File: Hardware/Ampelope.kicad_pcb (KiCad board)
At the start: 2 copper layers, 18.8 x 110 mm, 35 parts, among them J1 IN_A, J2 IN_B, J3 RM_OUT, J4 Eurorack_10_pin_power, U1 MC1496, U2 TL072

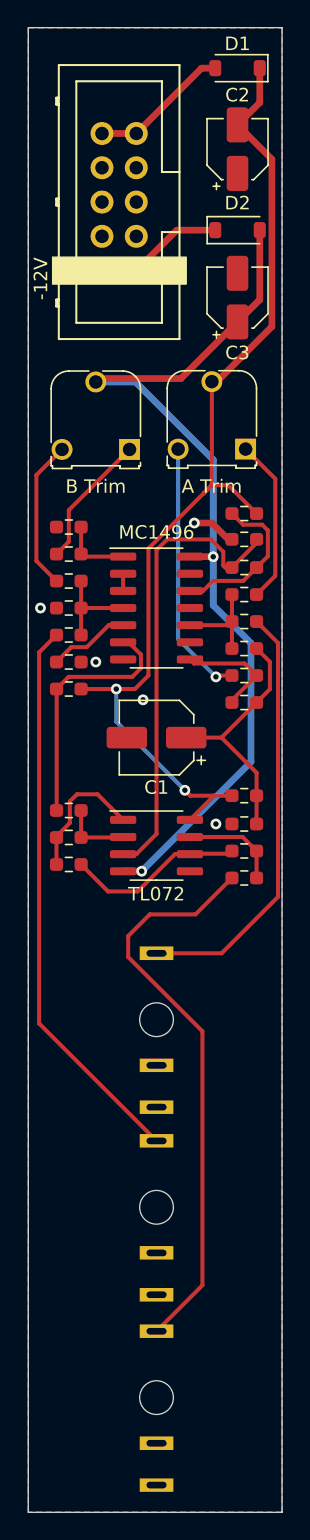
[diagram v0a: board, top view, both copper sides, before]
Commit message: Added STM32G431 project; clock configuration complete
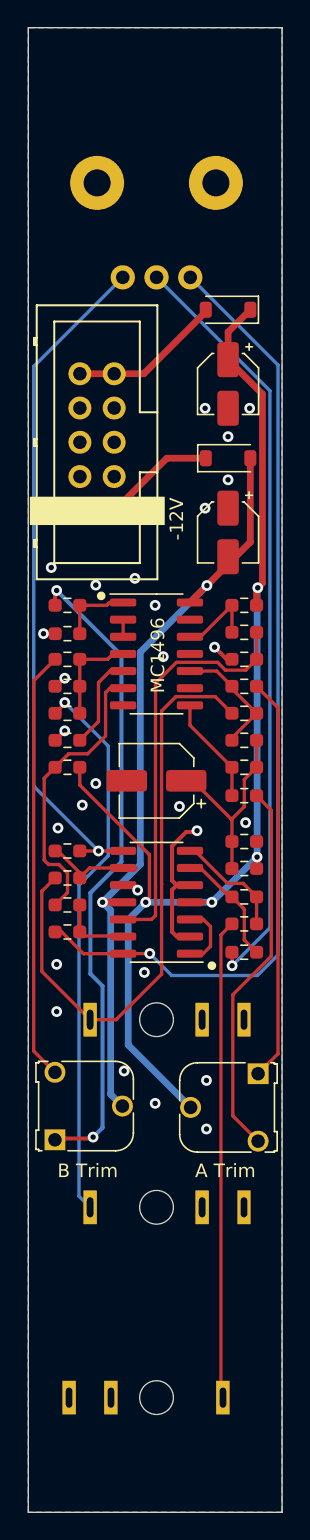
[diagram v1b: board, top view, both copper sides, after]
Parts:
- added R23: 15K, Resistor_SMD:R_0603_1608Metric_Pad0.98x0.95mm_HandSolder, F.Cu at (138.9, 100.0)
- added R24: 15K, Resistor_SMD:R_0603_1608Metric_Pad0.98x0.95mm_HandSolder, F.Cu at (138.9, 98.0)
- added RV3: R_Potentiometer, Custom_Footprints:Alpha_9mm_Potentiometer_Aligned, B.Cu at (145.5, 48.0)
- U2: value TL072 -> TL074; footprint Package_SO:SOIC-8_3.9x4.9mm_P1.27mm -> Package_SO:SOIC-14_3.9x8.7mm_P1.27mm
- moved RV2 51.4 mm to (138.0, 119.4), turned to 90 degrees
- moved RV1 46.3 mm to (153.0, 114.5), turned to -90 degrees
- moved D1 17.9 mm to (150.8, 57.9)
- moved J4 17.9 mm to (142.4, 72.8)
- moved C3 17.4 mm to (150.8, 74.4), turned to -90 degrees
- moved C2 17.4 mm to (150.8, 63.4), turned to -90 degrees
- moved D2 16.9 mm to (150.8, 68.9)
- moved R13 14.5 mm to (152.0, 105.5)
- moved R4 8.90 mm to (152.0, 93.9), turned to 180 degrees
- moved R18 8.89 mm to (152.0, 83.8)
- moved R22 7.90 mm to (138.9, 81.9)
- moved R12 7.00 mm to (138.9, 102.0)
- moved R6 7.00 mm to (138.9, 104.0)
- moved R11 6.80 mm to (152.0, 87.8), turned to 180 degrees
- moved R3 6.80 mm to (152.0, 85.8)
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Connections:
- C2 pad 1: GND -> VCC
- C2 pad 2: VCC -> GND
- C3 pad 1: VEE -> GND
- C3 pad 2: GND -> VEE
- R13 pad 2: Net-(R13-Pad2) -> /MIX_OUT
- R6 pad 1: Net-(R13-Pad2) -> /MIX_RM
- U2 pad 1: Net-(R13-Pad2) -> Net-(U2-Pad1)
- U2 pad 2: Net-(R12-Pad1) -> GND
- U2 pad 3: Net-(R15-Pad1) -> Net-(U2-Pad1)
- U2 pad 4: VEE -> VCC
- U2 pad 8: VCC -> Net-(R24-Pad1)
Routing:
- net /MIX_RM: track 0.00 -> 71.4 mm, vias 0 -> 1
- net /MIX_OUT: track 0.00 -> 56.6 mm, vias 0 -> 1
- net Net-(R24-Pad1): track 0.00 -> 50.4 mm, vias 0 -> 1
- net Net-(R21-Pad1): track 9.99 -> 48.2 mm, vias 0 -> 2
- net Net-(R20-Pad1): track 11.2 -> 31.9 mm
- net Net-(R3-Pad1): track 12.3 -> 30.0 mm
- net /A_IN: track 31.8 -> 44.7 mm
- net VEE: track 69.0 -> 56.5 mm
- net GND: track 3.29 -> 14.1 mm, vias 5 -> 28
- net Net-(R13-Pad2): track 10.0 -> 0.00 mm
- net VCC: track 77.0 -> 85.8 mm, vias 2 -> 4
- net Net-(R4-Pad1): track 19.3 -> 28.0 mm, vias 1 -> 0
- net Net-(R23-Pad1): track 0.00 -> 7.31 mm
- net Net-(J3-Pad3): track 42.4 -> 35.3 mm
- net Net-(R15-Pad2): track 11.9 -> 5.30 mm
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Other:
- board text added: "Ampelope Ring Mod v1 Mountjoy Modular"

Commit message: Preliminary pcb layout preparation
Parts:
- removed RV1: 500, Potentiometer_THT:Potentiometer_Runtron_RM-065_Vertical
- removed RV2: 220, Potentiometer_THT:Potentiometer_Runtron_RM-065_Vertical
- removed RV3: R_Potentiometer, Custom_Footprints:Alpha_9mm_Potentiometer_Aligned
- added C10: 22uF, Capacitor_SMD:CP_Elec_4x5.8, F.Cu at (1.25, 29.4)
- added C11: 100nF, Capacitor_SMD:C_0603_1608Metric_Pad1.08x0.95mm_HandSolder, F.Cu at (233.4, 43.1)
- added C12: 22uF, Capacitor_SMD:CP_Elec_4x5.8, F.Cu at (9.00, 29.4)
- added C13: 100nF, Capacitor_SMD:C_0603_1608Metric_Pad1.08x0.95mm_HandSolder, F.Cu at (229.1, 38.1)
- added C14: 10nF, Capacitor_SMD:C_0603_1608Metric_Pad1.08x0.95mm_HandSolder, F.Cu at (237.8, 45.6)
- added C15: 1uF, Capacitor_SMD:C_0603_1608Metric_Pad1.08x0.95mm_HandSolder, F.Cu at (233.4, 38.1)
- added C16: 560pF, Capacitor_SMD:C_0603_1608Metric_Pad1.08x0.95mm_HandSolder, F.Cu at (246.5, 38.1)
- added C17: 560pF, Capacitor_SMD:C_0603_1608Metric_Pad1.08x0.95mm_HandSolder, F.Cu at (233.4, 48.1)
- added C18: 560pF, Capacitor_SMD:C_0603_1608Metric_Pad1.08x0.95mm_HandSolder, F.Cu at (237.8, 40.6)
- added C19: 560pF, Capacitor_SMD:C_0603_1608Metric_Pad1.08x0.95mm_HandSolder, F.Cu at (233.4, 40.6)
- added C20: 10nF, Capacitor_SMD:C_0603_1608Metric_Pad1.08x0.95mm_HandSolder, F.Cu at (242.2, 40.6)
- added C21: 100nF, Capacitor_SMD:C_0603_1608Metric_Pad1.08x0.95mm_HandSolder, F.Cu at (237.8, 43.1)
- added C22: 100nF, Capacitor_SMD:C_0603_1608Metric_Pad1.08x0.95mm_HandSolder, F.Cu at (229.1, 45.6)
- added C23: 100pF, Capacitor_SMD:C_0603_1608Metric_Pad1.08x0.95mm_HandSolder, F.Cu at (246.5, 43.1)
- added C24: 100pF, Capacitor_SMD:C_0603_1608Metric_Pad1.08x0.95mm_HandSolder, F.Cu at (237.8, 48.1)
- added C25: 100pF, Capacitor_SMD:C_0603_1608Metric_Pad1.08x0.95mm_HandSolder, F.Cu at (229.1, 43.1)
- added C26: 100pF, Capacitor_SMD:C_0603_1608Metric_Pad1.08x0.95mm_HandSolder, F.Cu at (242.2, 43.1)
- added C4: 22uF, Capacitor_SMD:CP_Elec_4x5.8, F.Cu at (-74.8, 76.2)
- added C5: 100nF, Capacitor_SMD:C_0603_1608Metric_Pad1.08x0.95mm_HandSolder, F.Cu at (233.4, 45.6)
- added C6: 30pF, Capacitor_SMD:C_0603_1608Metric_Pad1.08x0.95mm_HandSolder, F.Cu at (229.1, 48.1)
- added C7: 30pF, Capacitor_SMD:C_0603_1608Metric_Pad1.08x0.95mm_HandSolder, F.Cu at (242.2, 38.1)
- added C8: 100nF, Capacitor_SMD:C_0603_1608Metric_Pad1.08x0.95mm_HandSolder, F.Cu at (246.5, 40.6)
- added C9: 22uF, Capacitor_SMD:CP_Elec_4x5.8, F.Cu at (-12.7, 53.7)
- added E1A_POT1: R_POT, Custom_Footprints:Alpha_9mm_Potentiometer_Aligned, F.Cu at (70.5, 32.5)
- added E1D_POT1: R_POT, Custom_Footprints:Alpha_9mm_Potentiometer_Aligned, F.Cu at (70.5, 51.5)
- added E1R_POT1: R_POT, Custom_Footprints:Alpha_9mm_Potentiometer_Aligned, F.Cu at (70.5, 89.5)
- added E1S_POT1: R_POT, Custom_Footprints:Alpha_9mm_Potentiometer_Aligned, F.Cu at (70.5, 70.5)
- added E1_MODE1: SW_SPDT_MSM, Custom_Footprints:SPDT_SubMiniature_Aligned, F.Cu at (85.0, 55.0)
- added E2A_POT1: R_POT, Custom_Footprints:Alpha_9mm_Potentiometer_Aligned, F.Cu at (111.5, 32.5)
- added E2D_POT1: R_POT, Custom_Footprints:Alpha_9mm_Potentiometer_Aligned, F.Cu at (111.5, 51.5)
- added E2R_POT1: R_POT, Custom_Footprints:Alpha_9mm_Potentiometer_Aligned, F.Cu at (111.3, 89.5)
- added E2S_POT1: R_POT, Custom_Footprints:Alpha_9mm_Potentiometer_Aligned, F.Cu at (111.3, 70.5)
- added E2_MODE1: SW_SPDT_MSM, Custom_Footprints:SPDT_SubMiniature_Aligned, F.Cu at (85.0, 71.5)
- added E3_MODE1: SW_SPDT_MSM, Custom_Footprints:SPDT_SubMiniature_Aligned, F.Cu at (85.0, 86.0)
- added E4_MODE1: SW_SPDT_MSM, Custom_Footprints:SPDT_SubMiniature_Aligned, F.Cu at (84.9, 100.0)
- added J10: Audio1_Out, Custom_Footprints:THONKICONN_hole, F.Cu at (85.0, 114.0)
- added J11: Audio2_Out, Custom_Footprints:THONKICONN_hole, F.Cu at (85.0, 127.0)
- added J12: Audio3_Out, Custom_Footprints:THONKICONN_hole, F.Cu at (115.0, 114.0)
- added J13: Audio4_Out, Custom_Footprints:THONKICONN_hole, F.Cu at (115.0, 127.0)
- added J14: Env1_Out, Custom_Footprints:THONKICONN_hole, F.Cu at (95.0, 55.5)
- added J15: Env2_Out, Custom_Footprints:THONKICONN_hole, F.Cu at (95.0, 69.5)
- added J16: Env3_Out, Custom_Footprints:THONKICONN_hole, F.Cu at (95.0, 84.0)
- added J17: Env4_Out, Custom_Footprints:THONKICONN_hole, F.Cu at (95.0, 99.0)
- added J18: SWD_Header, Custom_Footprints:SWD_header, F.Cu at (-88.2, 75.1)
- added J19: USB_B_Micro, Custom_Footprints:USB_Micro-B_Amphenol, F.Cu at (-34.1, 57.7)
- added J5: Gate4_In, Custom_Footprints:THONKICONN_hole, F.Cu at (95.0, 127.0)
- added J6: Audio1_In, Custom_Footprints:THONKICONN_hole, F.Cu at (65.0, 114.0)
- added J7: Audio2_In, Custom_Footprints:THONKICONN_hole, F.Cu at (75.0, 127.0)
- added J8: Audio3_In, Custom_Footprints:THONKICONN_hole, F.Cu at (105.0, 113.9)
- added J9: Audio4_In, Custom_Footprints:THONKICONN_hole, F.Cu at (105.0, 127.0)
- added L1: L_Small, Inductor_SMD:L_0805_2012Metric_Pad1.05x1.20mm_HandSolder, F.Cu at (244.5, 132.8)
- added LED1: LED, LED_THT:LED_D3.0mm, F.Cu at (90.2, 48.0)
- added LED2: LED, LED_THT:LED_D3.0mm, F.Cu at (83.7, 64.5)
- added LED3: LED, LED_THT:LED_D3.0mm, F.Cu at (84.0, 79.0)
- added LED4: LED, LED_THT:LED_D3.0mm, F.Cu at (84.0, 93.0)
- added LFO_POT1: R_POT, Custom_Footprints:Alpha_9mm_Potentiometer_Aligned, F.Cu at (91.5, 32.5)
- added Q1: MMBT3904, Package_TO_SOT_SMD:SOT-23, F.Cu at (19.4, 14.7)
- added Q2: MMBT3904, Package_TO_SOT_SMD:SOT-23, F.Cu at (-0.18, 34.6)
- added Q3: MMBT3904, Package_TO_SOT_SMD:SOT-23, F.Cu at (-27.4, 64.8)
- added Q4: MMBT3904, Package_TO_SOT_SMD:SOT-23, F.Cu at (9.97, 21.2)
- added R25: 10k, Resistor_SMD:R_0603_1608Metric_Pad0.98x0.95mm_HandSolder, F.Cu at (250.8, 86.5)
- added R26: 10k, Resistor_SMD:R_0603_1608Metric_Pad0.98x0.95mm_HandSolder, F.Cu at (237.8, 89.0)
- added R27: 30k, Resistor_SMD:R_0603_1608Metric_Pad0.98x0.95mm_HandSolder, F.Cu at (242.2, 99.1)
- added R28: 30k, Resistor_SMD:R_0603_1608Metric_Pad0.98x0.95mm_HandSolder, F.Cu at (250.8, 96.6)
- added R29: 30k, Resistor_SMD:R_0603_1608Metric_Pad0.98x0.95mm_HandSolder, F.Cu at (237.8, 86.5)
- added R30: 30k, Resistor_SMD:R_0603_1608Metric_Pad0.98x0.95mm_HandSolder, F.Cu at (246.5, 91.6)
- added R31: 1k, Resistor_SMD:R_0603_1608Metric_Pad0.98x0.95mm_HandSolder, F.Cu at (255.2, 86.5)
- added R32: 1k, Resistor_SMD:R_0603_1608Metric_Pad0.98x0.95mm_HandSolder, F.Cu at (250.8, 91.6)
- added R33: 1k, Resistor_SMD:R_0603_1608Metric_Pad0.98x0.95mm_HandSolder, F.Cu at (233.4, 84.0)
- added R34: 1k, Resistor_SMD:R_0603_1608Metric_Pad0.98x0.95mm_HandSolder, F.Cu at (237.8, 99.1)
- added R35: 75k, Resistor_SMD:R_0603_1608Metric_Pad0.98x0.95mm_HandSolder, F.Cu at (242.2, 96.6)
- added R36: 20k, Resistor_SMD:R_0603_1608Metric_Pad0.98x0.95mm_HandSolder, F.Cu at (242.2, 94.1)
- added R37: 75k, Resistor_SMD:R_0603_1608Metric_Pad0.98x0.95mm_HandSolder, F.Cu at (263.9, 84.0)
- added R38: 20k, Resistor_SMD:R_0603_1608Metric_Pad0.98x0.95mm_HandSolder, F.Cu at (263.9, 86.5)
- added R39: 75k, Resistor_SMD:R_0603_1608Metric_Pad0.98x0.95mm_HandSolder, F.Cu at (242.2, 91.6)
- added R40: 20k, Resistor_SMD:R_0603_1608Metric_Pad0.98x0.95mm_HandSolder, F.Cu at (242.2, 89.0)
- added R41: 75k, Resistor_SMD:R_0603_1608Metric_Pad0.98x0.95mm_HandSolder, F.Cu at (242.2, 86.5)
- added R42: 20k, Resistor_SMD:R_0603_1608Metric_Pad0.98x0.95mm_HandSolder, F.Cu at (255.2, 96.6)
- added R43: 47k, Resistor_SMD:R_0603_1608Metric_Pad0.98x0.95mm_HandSolder, F.Cu at (242.2, 101.6)
- added R44: 47k, Resistor_SMD:R_0603_1608Metric_Pad0.98x0.95mm_HandSolder, F.Cu at (246.5, 96.6)
- added R45: 47k, Resistor_SMD:R_0603_1608Metric_Pad0.98x0.95mm_HandSolder, F.Cu at (250.8, 99.1)
- added R46: 47k, Resistor_SMD:R_0603_1608Metric_Pad0.98x0.95mm_HandSolder, F.Cu at (246.5, 89.0)
- added R47: 1k, Resistor_SMD:R_0603_1608Metric_Pad0.98x0.95mm_HandSolder, F.Cu at (259.6, 84.0)
- added R48: 1k, Resistor_SMD:R_0603_1608Metric_Pad0.98x0.95mm_HandSolder, F.Cu at (233.4, 99.1)
- added R49: 1k, Resistor_SMD:R_0603_1608Metric_Pad0.98x0.95mm_HandSolder, F.Cu at (246.5, 86.5)
- added R50: 1k, Resistor_SMD:R_0603_1608Metric_Pad0.98x0.95mm_HandSolder, F.Cu at (237.8, 91.6)
- added RESET1: SW_Push, Custom_Footprints:SW_PUSH_6mm_aligned, F.Cu at (-64.4, 75.8)
- added U3: LM1117-3.3, Package_TO_SOT_SMD:SOT-223-3_TabPin2, F.Cu at (250.5, 165.1)
- added U4: TL074, Package_SO:SOIC-14_3.9x8.7mm_P1.27mm, F.Cu at (-20.8, 45.7)
- added U5: TL074, Package_SO:SOIC-14_3.9x8.7mm_P1.27mm, F.Cu at (-12.3, 45.7)
- added U6: TL074, Package_SO:SOIC-14_3.9x8.7mm_P1.27mm, F.Cu at (-20.8, 55.9)
- added Y1: 8MHz 20pF, Crystal:Crystal_SMD_5032-2Pin_5.0x3.2mm_HandSoldering, F.Cu at (240.4, 163.4)
- C1: value 100uF 16V -> 1uF; footprint Capacitor_SMD:CP_Elec_5x5.7 -> Capacitor_SMD:C_0603_1608Metric_Pad1.08x0.95mm_HandSolder
- C2: value 22uF -> 4.7uF; footprint Capacitor_SMD:CP_Elec_4x5.8 -> Capacitor_SMD:C_0603_1608Metric_Pad1.08x0.95mm_HandSolder
- C3: value 22uF -> 100nF; footprint Capacitor_SMD:CP_Elec_4x5.8 -> Capacitor_SMD:C_0603_1608Metric_Pad1.08x0.95mm_HandSolder
- J1: value IN_A -> Eurorack_10_pin_power; footprint Custom_Footprints:THONKICONN_hole -> Custom_Footprints:Eurorack_10_pin_header; moved to F.Cu
- J2: value IN_B -> Gate1_In; moved to F.Cu
- J3: value RM_OUT -> Gate2_In; moved to F.Cu
- J4: value Eurorack_10_pin_power -> Gate3_In; footprint Custom_Footprints:Eurorack_10_pin_header -> Custom_Footprints:THONKICONN_hole
- R1: value 1K5 -> 100k
- R10: value 68K -> 1k
- R11, R16: value 180K -> 1k
- R12, R15, R18: value 15K -> 1k
- R13: value 10K -> 1k
- R14: value 470 -> 100R
- R17: value 6K8 -> 1k
- R19, R22: value 2K7 -> 10k
- R2: value 1K5 -> 30k
- R20, R21: value 6K8 -> 10k
- R23, R24: value 15K -> 10k
- R3: value 12K -> 30k
- R4: value 12K -> 510R
- R5: value 2K7 -> 30k
- R6: value 15K -> 30k
- R7: value 2K7 -> 510R
- R8, R9: value 1K2 -> 510R
- U1: value MC1496 -> STM32G431RB; footprint Package_SO:SOIC-14_3.9x8.7mm_P1.27mm -> Package_QFP:LQFP-64_10x10mm_P0.5mm
- U2: value TL074 -> AS3364; footprint Package_SO:SOIC-14_3.9x8.7mm_P1.27mm -> Package_SO:SOIC-16_3.9x9.9mm_P1.27mm
- moved J1 254.8 mm to (-92.4, 19.2), turned to 0 degrees
- moved U2 241.2 mm to (-94.2, 75.6), turned to 0 degrees
- moved D1 238.3 mm to (-87.2, 71.5), turned to 0 degrees
- moved D2 236.1 mm to (-81.2, 25.2)
- moved U1 223.1 mm to (-76.9, 66.0)
- moved R17 116.4 mm to (255.2, 84.0)
- moved R8 112.0 mm to (250.8, 89.0), turned to 0 degrees
- moved R22 109.4 mm to (246.5, 101.6)
- moved R14 108.5 mm to (259.6, 89.0)
- moved R24 108.5 mm to (246.5, 84.0), turned to 0 degrees
- moved R2 108.3 mm to (259.6, 86.5), turned to 0 degrees
- moved R6 108.1 mm to (246.5, 94.1)
- moved C1 107.3 mm to (237.8, 38.1), turned to 0 degrees
- moved R13 104.5 mm to (255.2, 89.0), turned to 0 degrees
- moved R21 103.3 mm to (242.2, 84.0)
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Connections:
- C1 pad 1: Net-(C1-Pad1) -> GND
- C1 pad 2: GND -> +3.3VA
- C2 pad 1: VCC -> GND
- C2 pad 2: GND -> +3V3
- C3 pad 2: VEE -> +3.3VA
- J1 pad 1: GND -> -12V
- J1 pad 2: GND -> -12V
- J1 pad 3: /A_IN -> GND
- J2 pad 2: GND -> unconnected-(J2-Pad2)
- J2 pad 3: Net-(J2-Pad3) -> /Gate1
- J3 pad 2: unconnected-(J3-Pad2) -> /Gate1
- J3 pad 3: Net-(J3-Pad3) -> /Gate2
- J4 pad 1: -12V -> GND
- J4 pad 2: -12V -> /Gate2
- J4 pad 3: GND -> /Gate3
- R1 pad 1: Net-(C1-Pad1) -> GND
- R1 pad 2: GND -> Net-(R1-Pad2)
- R10 pad 1: Net-(R10-Pad1) -> /Gate1
- R10 pad 2: Net-(R10-Pad2) -> Net-(Q1-Pad1)
- R11 pad 1: Net-(R11-Pad1) -> /Gate2
- R11 pad 2: /A_IN -> Net-(Q2-Pad1)
- R12 pad 1: Net-(R12-Pad1) -> /Gate3
- R12 pad 2: Net-(R12-Pad2) -> Net-(Q3-Pad1)
- R13 pad 1: Net-(R10-Pad2) -> Net-(J5-Pad3)
- R13 pad 2: /MIX_OUT -> Net-(Q4-Pad1)
- R14 pad 1: Net-(J3-Pad3) -> Net-(C20-Pad1)
- R14 pad 2: Net-(R10-Pad1) -> Net-(R14-Pad2)
- R15 pad 1: Net-(R15-Pad1) -> /Gate1_Inv
- R15 pad 2: Net-(R15-Pad2) -> +3V3
- R16 pad 1: Net-(R16-Pad1) -> /Gate2_Inv
- R16 pad 2: Net-(J2-Pad3) -> +3V3
- R17 pad 1: GND -> /Gate3_Inv
- R17 pad 2: Net-(R17-Pad2) -> +3V3
- R18 pad 1: GND -> /Gate4_Inv
- R18 pad 2: Net-(R15-Pad1) -> +3V3
- R19 pad 1: GND -> Net-(R19-Pad1)
- R19 pad 2: Net-(R16-Pad1) -> GND
- R2 pad 1: VCC -> Net-(R2-Pad1)
- R2 pad 2: Net-(C1-Pad1) -> /Audio3_In_Buff
- R20 pad 2: Net-(R16-Pad1) -> GND
- R21 pad 2: Net-(R21-Pad2) -> GND
- R22 pad 1: GND -> Net-(R22-Pad1)
- R22 pad 2: Net-(R21-Pad2) -> GND
- R23 pad 1: Net-(R23-Pad1) -> /Audio1_In_Buff
- R23 pad 2: /A_IN -> Net-(R19-Pad1)
- R24 pad 1: Net-(R24-Pad1) -> /Audio2_In_Buff
- R24 pad 2: Net-(R23-Pad1) -> Net-(R20-Pad1)
- R3 pad 2: Net-(R11-Pad1) -> /Audio4_In_Buff
- R4 pad 2: Net-(R4-Pad2) -> Net-(R2-Pad1)
- R5 pad 1: Net-(R4-Pad2) -> Net-(R5-Pad1)
- R5 pad 2: Net-(C1-Pad1) -> /Audio1_In_Buff
- R6 pad 1: /MIX_RM -> Net-(R6-Pad1)
- R6 pad 2: Net-(R12-Pad1) -> /Audio2_In_Buff
- R7 pad 1: Net-(R11-Pad1) -> Net-(C17-Pad1)
- R7 pad 2: Net-(C1-Pad1) -> Net-(R3-Pad1)
- R8 pad 1: VCC -> Net-(C18-Pad1)
- R8 pad 2: Net-(R12-Pad2) -> Net-(R5-Pad1)
- R9 pad 1: VCC -> Net-(C19-Pad1)
- R9 pad 2: Net-(R15-Pad2) -> Net-(R6-Pad1)
- U1 pad 1: Net-(R21-Pad2) -> +3V3
- U1 pad 10: Net-(R11-Pad1) -> /EnvA_Sustain
- U1 pad 11: unconnected-(U1-Pad11) -> /EnvA_Release
- U1 pad 12: Net-(R15-Pad2) -> /EnvB_Attack
- U1 pad 13: unconnected-(U1-Pad13) -> /EnvB_Decay
- U1 pad 14: VEE -> /Env3_DAC
- U1 pad 2: Net-(U1-Pad2) -> unconnected-(U1-Pad2)
- U1 pad 3: Net-(U1-Pad2) -> unconnected-(U1-Pad3)
- U1 pad 4: Net-(R16-Pad1) -> unconnected-(U1-Pad4)
- U1 pad 5: Net-(R17-Pad2) -> Net-(C6-Pad2)
- U1 pad 6: Net-(R12-Pad2) -> Net-(C7-Pad2)
- U1 pad 7: unconnected-(U1-Pad7) -> /RESET
- U1 pad 8: Net-(R4-Pad2) -> /EnvA_Attack
- U1 pad 9: unconnected-(U1-Pad9) -> /EnvA_Decay
- U2 pad 1: Net-(U2-Pad1) -> Net-(R14-Pad2)
- U2 pad 10: GND -> Net-(R2-Pad1)
- U2 pad 11: VEE -> /Env3_DAC
- U2 pad 12: Net-(R15-Pad1) -> /Audio3_VCA
- U2 pad 13: Net-(R12-Pad1) -> /Audio4_VCA
- U2 pad 14: /MIX_RM -> /Env4_DAC
- U2 pad 2: GND -> Net-(R5-Pad1)
- U2 pad 3: Net-(U2-Pad1) -> /Env1_DAC
- U2 pad 4: VCC -> /Audio1_VCA
- U2 pad 5: GND -> /Audio2_VCA
- U2 pad 6: Net-(R10-Pad2) -> /Env2_DAC
- U2 pad 7: Net-(R10-Pad1) -> Net-(R6-Pad1)
- U2 pad 8: Net-(R24-Pad1) -> GND
- U2 pad 9: Net-(R23-Pad1) -> VEE
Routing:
- net VCC: track 85.8 -> 0.00 mm, vias 4 -> 0
- net /MIX_RM: track 71.4 -> 0.00 mm, vias 1 -> 0
- net /MIX_OUT: track 56.6 -> 0.00 mm, vias 1 -> 0
- net VEE: track 56.5 -> 0.00 mm, vias 2 -> 0
- net Net-(R24-Pad1): track 50.4 -> 0.00 mm, vias 1 -> 0
- net Net-(R21-Pad1): track 48.2 -> 0.00 mm, vias 2 -> 0
- net /A_IN: track 44.7 -> 0.00 mm
- net Net-(J2-Pad3): track 41.1 -> 0.00 mm, vias 1 -> 0
- net Net-(J3-Pad3): track 35.3 -> 0.00 mm
- net Net-(R20-Pad1): track 31.9 -> 0.00 mm
- net Net-(R15-Pad1): track 30.4 -> 0.00 mm
- net Net-(R3-Pad1): track 30.0 -> 0.00 mm
- net Net-(C16-Pad1): track 28.0 -> 0.00 mm
- net Net-(R12-Pad2): track 21.4 -> 0.00 mm
- net Net-(C1-Pad1): track 14.8 -> 0.00 mm
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- removed copper zone on B.Cu, net GND
- removed copper zone on F.Cu, net GND
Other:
- board size 18.8 x 110 mm -> 71 x 110 mm
- board text removed: "A Trim"
- board text removed: "Ampelope Ring Mod v1 Mountjoy Modular"
- board text removed: "B Trim"
